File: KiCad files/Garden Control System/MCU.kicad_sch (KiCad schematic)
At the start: 24 parts, among them SW1 SW_SPDT, U1 STM32F207ZGTx, Y1 16MHz

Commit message: Close to finishing ethernet side
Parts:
- removed Y1: 16MHz, symbol Device:Crystal_GND24
- added R1: 0, symbol Device:R
- added Y1: ECS-160-8-37-CWY-TR3, ECS-160-8-37-CWY-TR3:XTAL_ECS-160-8-37-CWY-TR3, symbol ECS-160-8-37-CWY-TR3:ECS-160-8-37-CWY-TR3
- renumbered C1 to C10, C1 to C11, C1 to C12, C1 to C13, C2 to C14, C1 to C15, C1 to C16, C1 to C17, C1 to C18, C1 to C19, C1 to C2, C1 to C3, C1 to C4, C1 to C5, C1 to C6, C1 to C7, C1 to C8, C1 to C9, R1 to R6, SW1 to SW2
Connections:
- net GND: now also Y1.2 (GND), Y1.4 (GND__1)
- net HSE IN: now also Y1.1 (IN/OUT)
- net HSE OUT: now also R1.1; no longer C11.1
- net MII_TXD3: now reaches U1.1 (PE2)
- net MII_MDC: now reaches U1.27 (PC1)
- net MII_TXD2: now reaches U1.28 (PC2)
- net MII_TX_CLK: now reaches U1.29 (PC3)
- net MII_CRS: now reaches U1.34 (PA0)
- net MII_RX_CLK: now reaches U1.35 (PA1)
- net MII_COL: now reaches U1.37 (PA3)
- net MII_RX_DV: now reaches U1.43 (PA7)
- net MII_RX_RD0: now reaches U1.44 (PC4)
- net MII_RX_RD1: now reaches U1.45 (PC5)
- net MII_RX_RD2: now reaches U1.46 (PB0)
- net MII_RX_RD3: now reaches U1.47 (PB1)
- net MII_TXD0: now reaches U1.73 (PB12)
- net MII_TXD1: now reaches U1.74 (PB13)
- new net: C11.1, R1.2, Y1.3 (OUT/IN)
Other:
- moved on the sheet: C11, C12

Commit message: working on power arch
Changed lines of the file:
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@@
+		)
+	)
+	(global_label "MCU_I_SENSE0"
+		(shape input)
+		(at 207.01 124.46 0)
+		(fields_autoplaced yes)
+		(effects
+			(font
+				(size 1.27 1.27)
+			)
+			(justify left)
+		)
+		(property "Intersheetrefs" "${INTERSHEET_REFS}"
+			(at 223.8441 124.46 0)
+			(effects
+				(font
+					(size 1.27 1.27)
+				)
+				(justify left)
+				(hide yes)
+			)
 		)
 	)
@@
 		)
 	)
+	(global_label "MCU_I_SENSE2"
+		(shape input)
+		(at 207.01 129.54 0)
+		(fields_autoplaced yes)
+		(effects
+			(font
+				(size 1.27 1.27)
+			)
+			(justify left)
+		)
+		(property "Intersheetrefs" "${INTERSHEET_REFS}"
+			(at 223.8441 129.54 0)
+			(effects
+				(font
+					(size 1.27 1.27)
+				)
+				(justify left)
+				(hide yes)
+			)
+		)
+	)
+	(global_label "M1_PWM"
+		(shape input)
+		(at 207.01 111.76 0)
+		(fields_autoplaced yes)
+		(effects
+			(font
+				(size 1.27 1.27)
+			)
+			(justify left)
+		)
+		(property "Intersheetrefs" "${INTERSHEET_REFS}"
+			(at 217.7965 111.76 0)
+			(effects
+				(font
+					(size 1.27 1.27)
+				)
+				(justify left)
+				(hide yes)
+			)
+		)
+	)
 	(global_label "MII_RX_RD2"
 		(shape input)
@@
 		)
 	)
+	(global_label "M0_PWM"
+		(shape input)
+		(at 207.01 109.22 0)
+		(fields_autoplaced yes)
+		(effects
+			(font
+				(size 1.27 1.27)
+			)
+			(justify left)
+		)
+		(property "Intersheetrefs" "${INTERSHEET_REFS}"
+			(at 217.7965 109.22 0)
+			(effects
+				(font
+					(size 1.27 1.27)
+				)
+				(justify left)
+				(hide yes)
+			)
+		)
+	)
 	(global_label "HSE OUT"
 		(shape input)
@@
 			(effects
 				(font
+					(size 1.27 1.27)
+				)
+				(justify left)
+				(hide yes)
+			)
+		)
+	)
+	(global_label "MCU_I_SENSE3"
+		(shape input)
+		(at 207.01 132.08 0)
+		(fields_autoplaced yes)
+		(effects
+			(font
+				(size 1.27 1.27)
+			)
+			(justify left)
+		)
+		(property "Intersheetrefs" "${INTERSHEET_REFS}"
+			(at 223.8441 132.08 0)
+			(effects
+				(font
+					(size 1.27 1.27)
+				)
+				(justify left)
+				(hide yes)
+			)
+		)
+	)
+	(global_label "M2_PWM"
+		(shape input)
+		(at 207.01 114.3 0)
+		(fields_autoplaced yes)
+		(effects
+			(font
+				(size 1.27 1.27)
+			)
+			(justify left)
+		)
+		(property "Intersheetrefs" "${INTERSHEET_REFS}"
+			(at 217.7965 114.3 0)
+			(effects
+				(font
+					(size 1.27 1.27)
+				)
+				(justify left)
+				(hide yes)
+			)
+		)
+	)
+	(global_label "MCU_I_SENSE1"
+		(shape input)
+		(at 207.01 127 0)
+		(fields_autoplaced yes)
+		(effects
+			(font
+				(size 1.27 1.27)
+			)
+			(justify left)
+		)
+		(property "Intersheetrefs" "${INTERSHEET_REFS}"
+			(at 223.8441 127 0)
+			(effects
+				(font

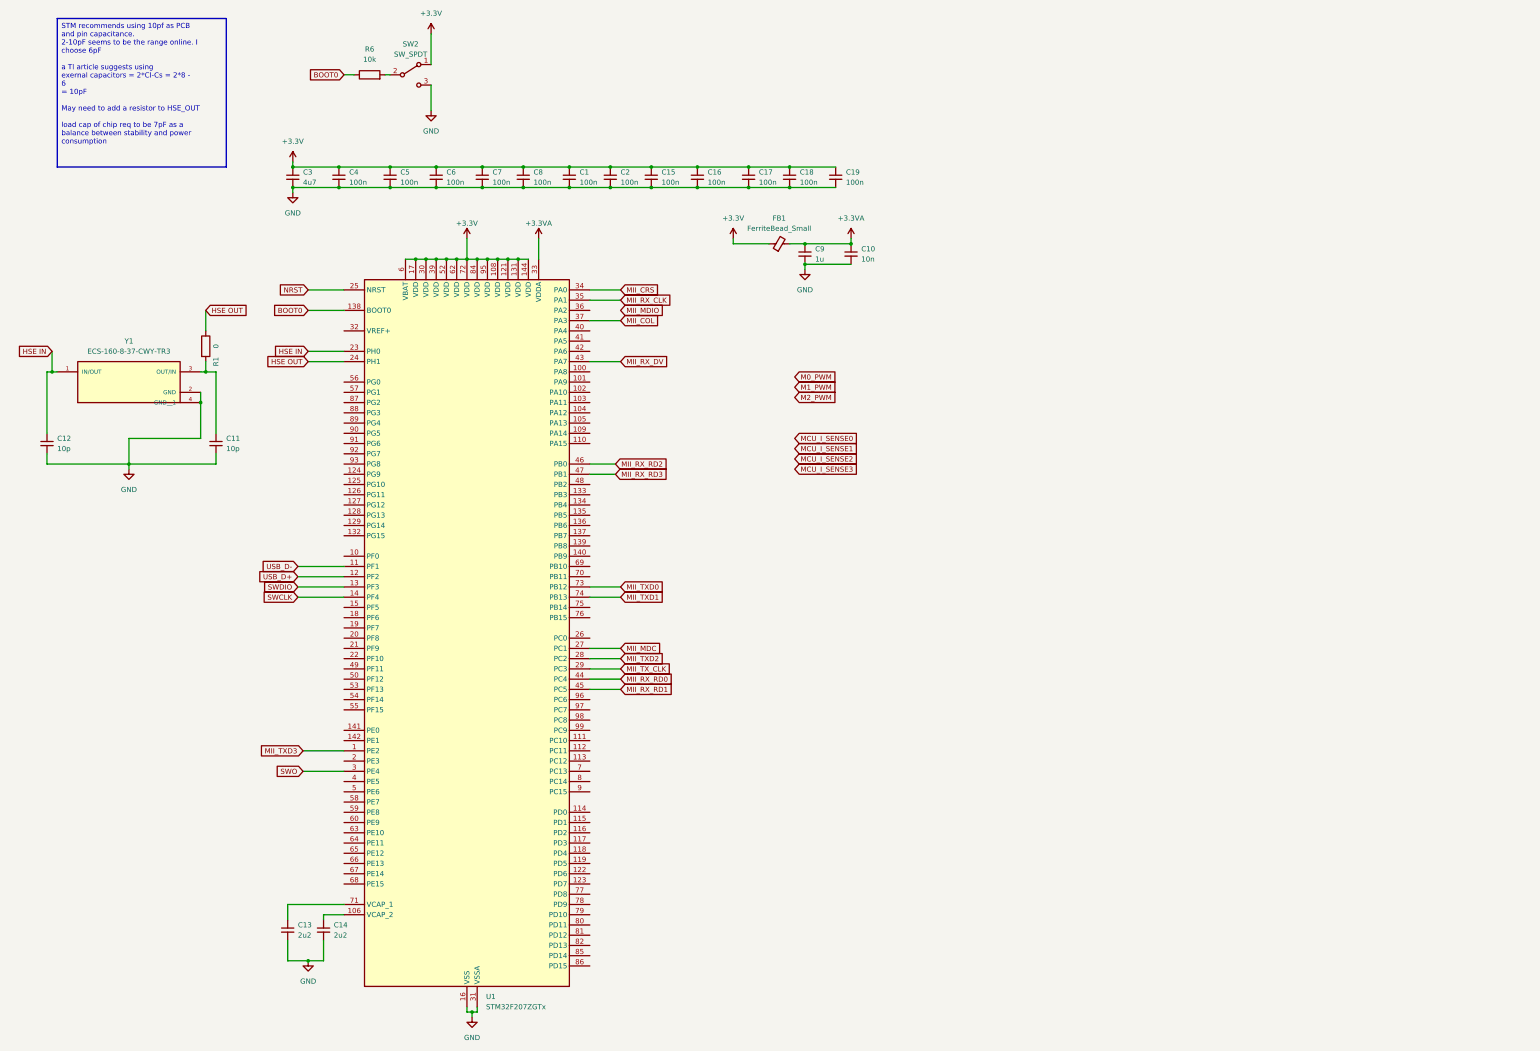
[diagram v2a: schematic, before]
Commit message: expanded power supply section. completed LSD design. sized shunt resistors
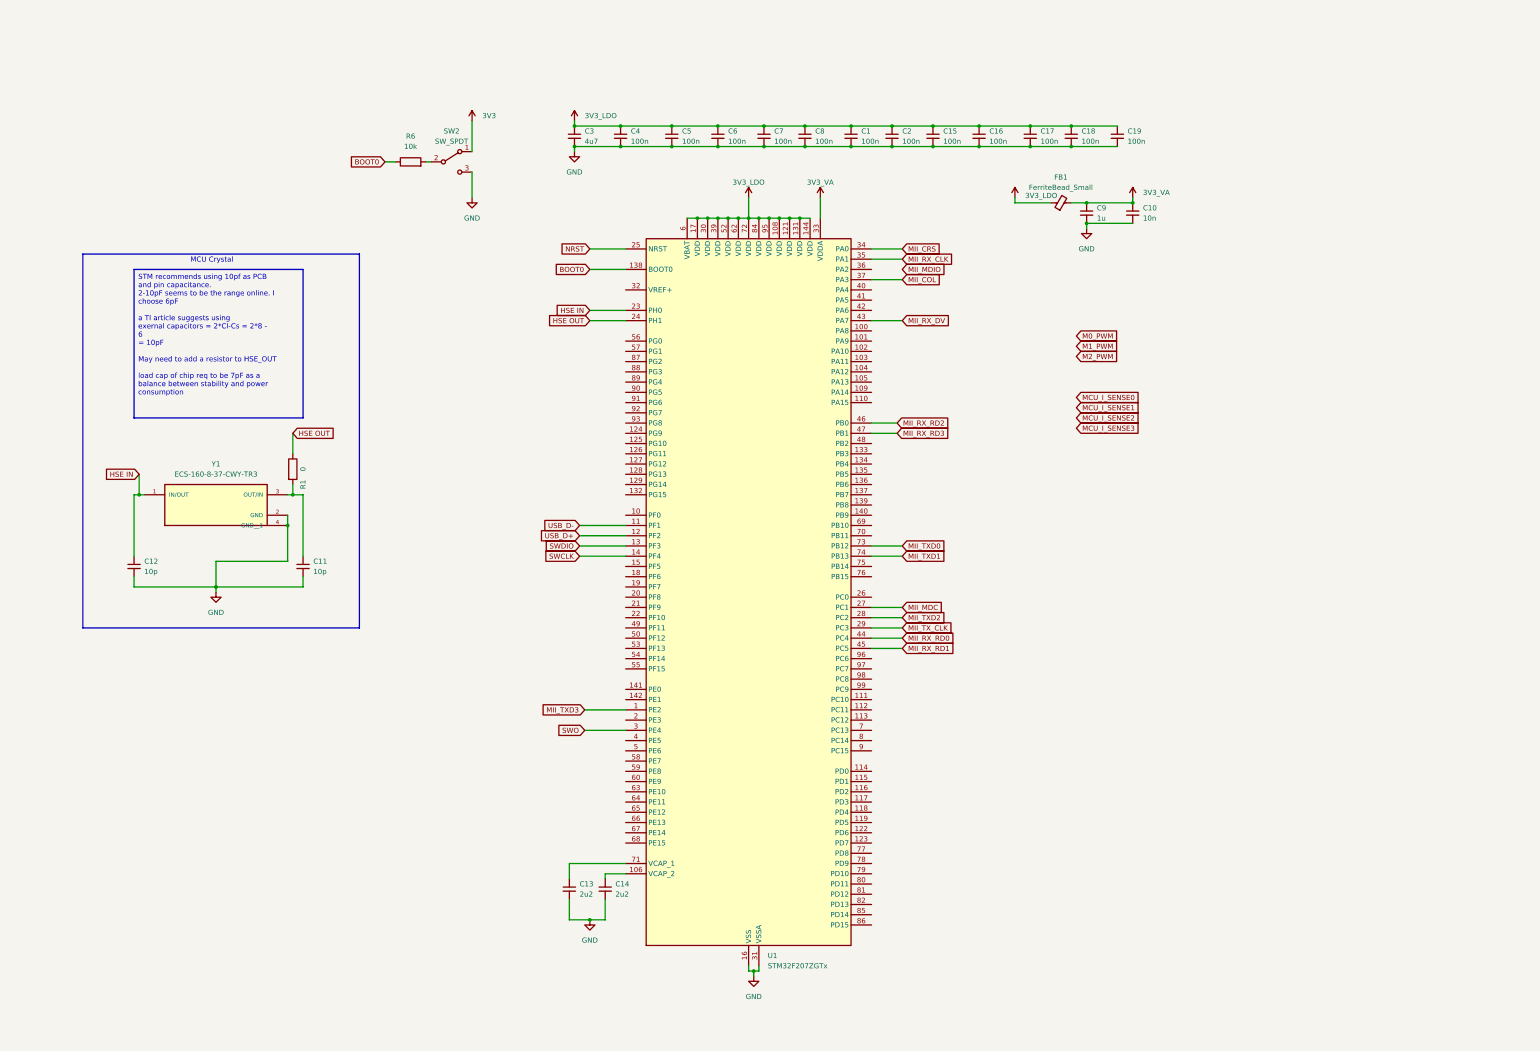
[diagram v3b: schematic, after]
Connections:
- net +3.3V renamed 3V3_LDO
- net 3V3_LDO: no longer SW2.1 (A)
- net +3.3VA renamed 3V3_VA
- new net 3V3: SW2.1 (A)
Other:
- note added: "MCU Crystal"
- moved on the sheet: C1, C10, C11, C12, C13, C14, C15, C16, C17, C18, C19, C2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

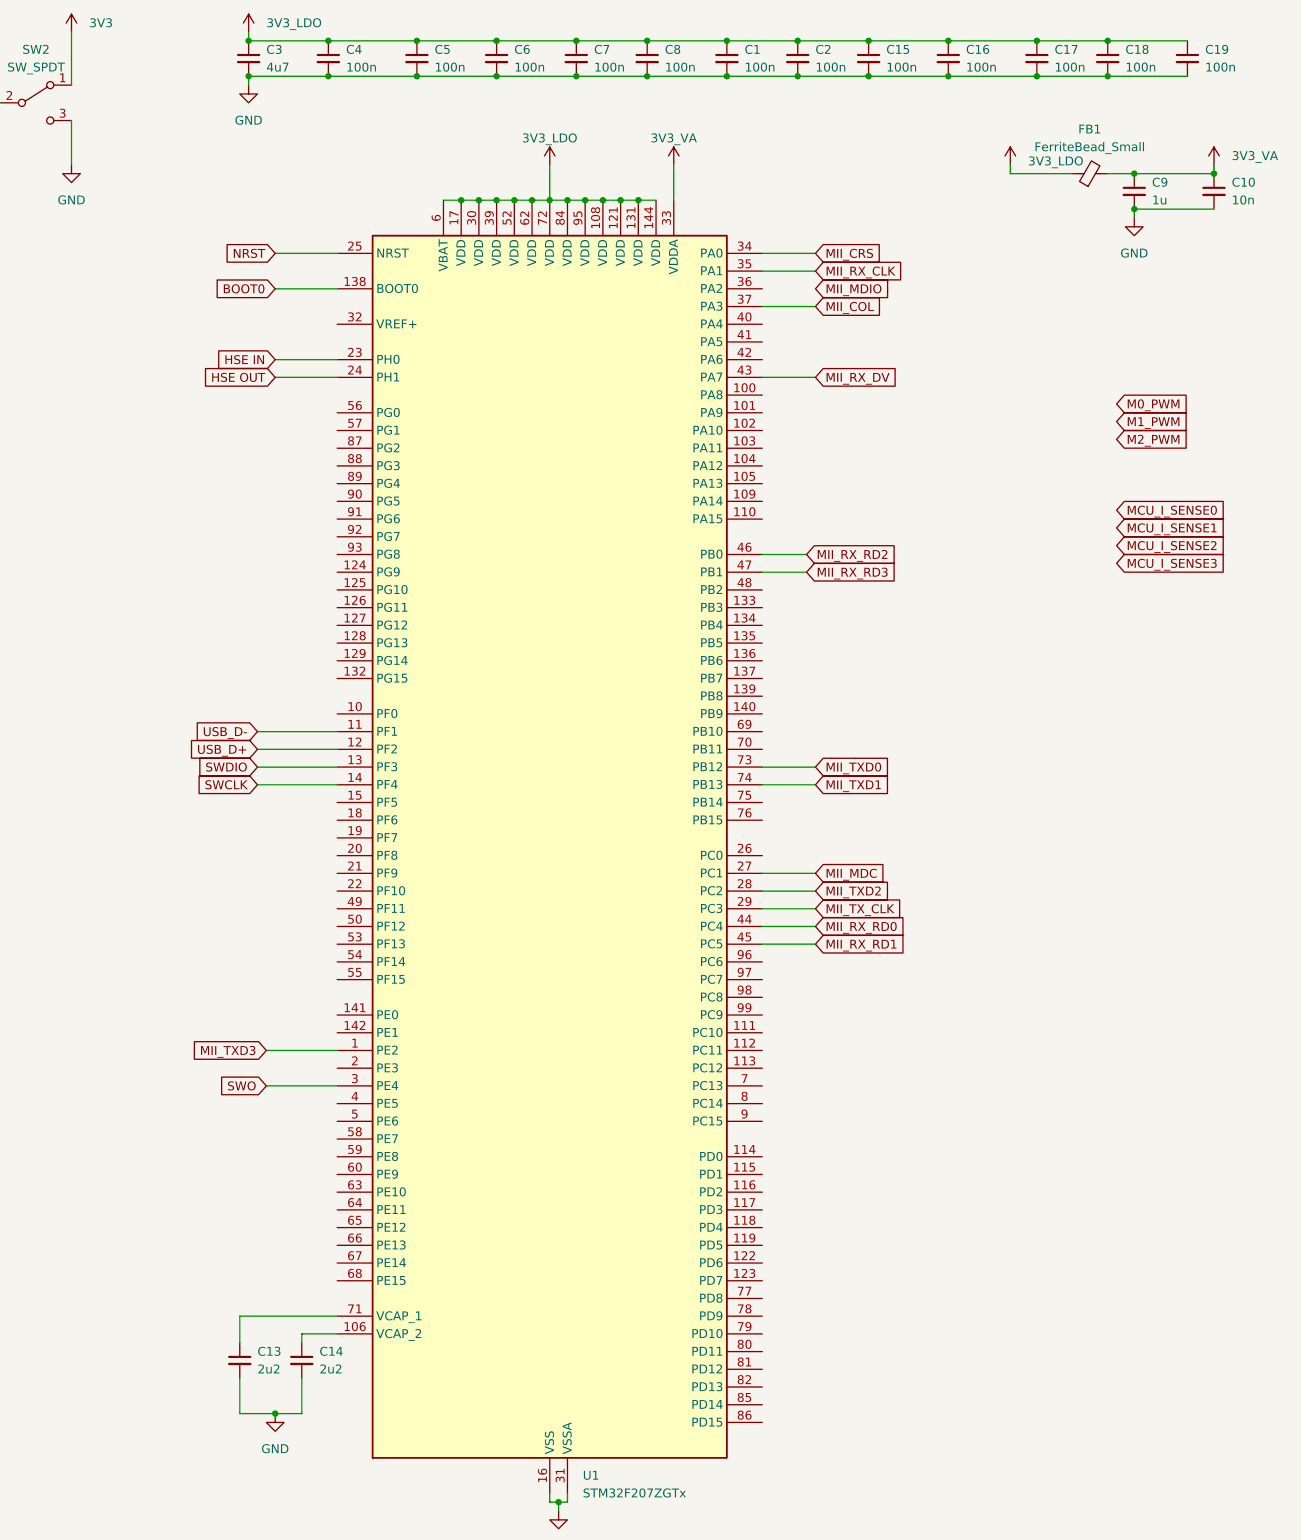
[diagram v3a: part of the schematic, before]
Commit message: adding recent schematic progress
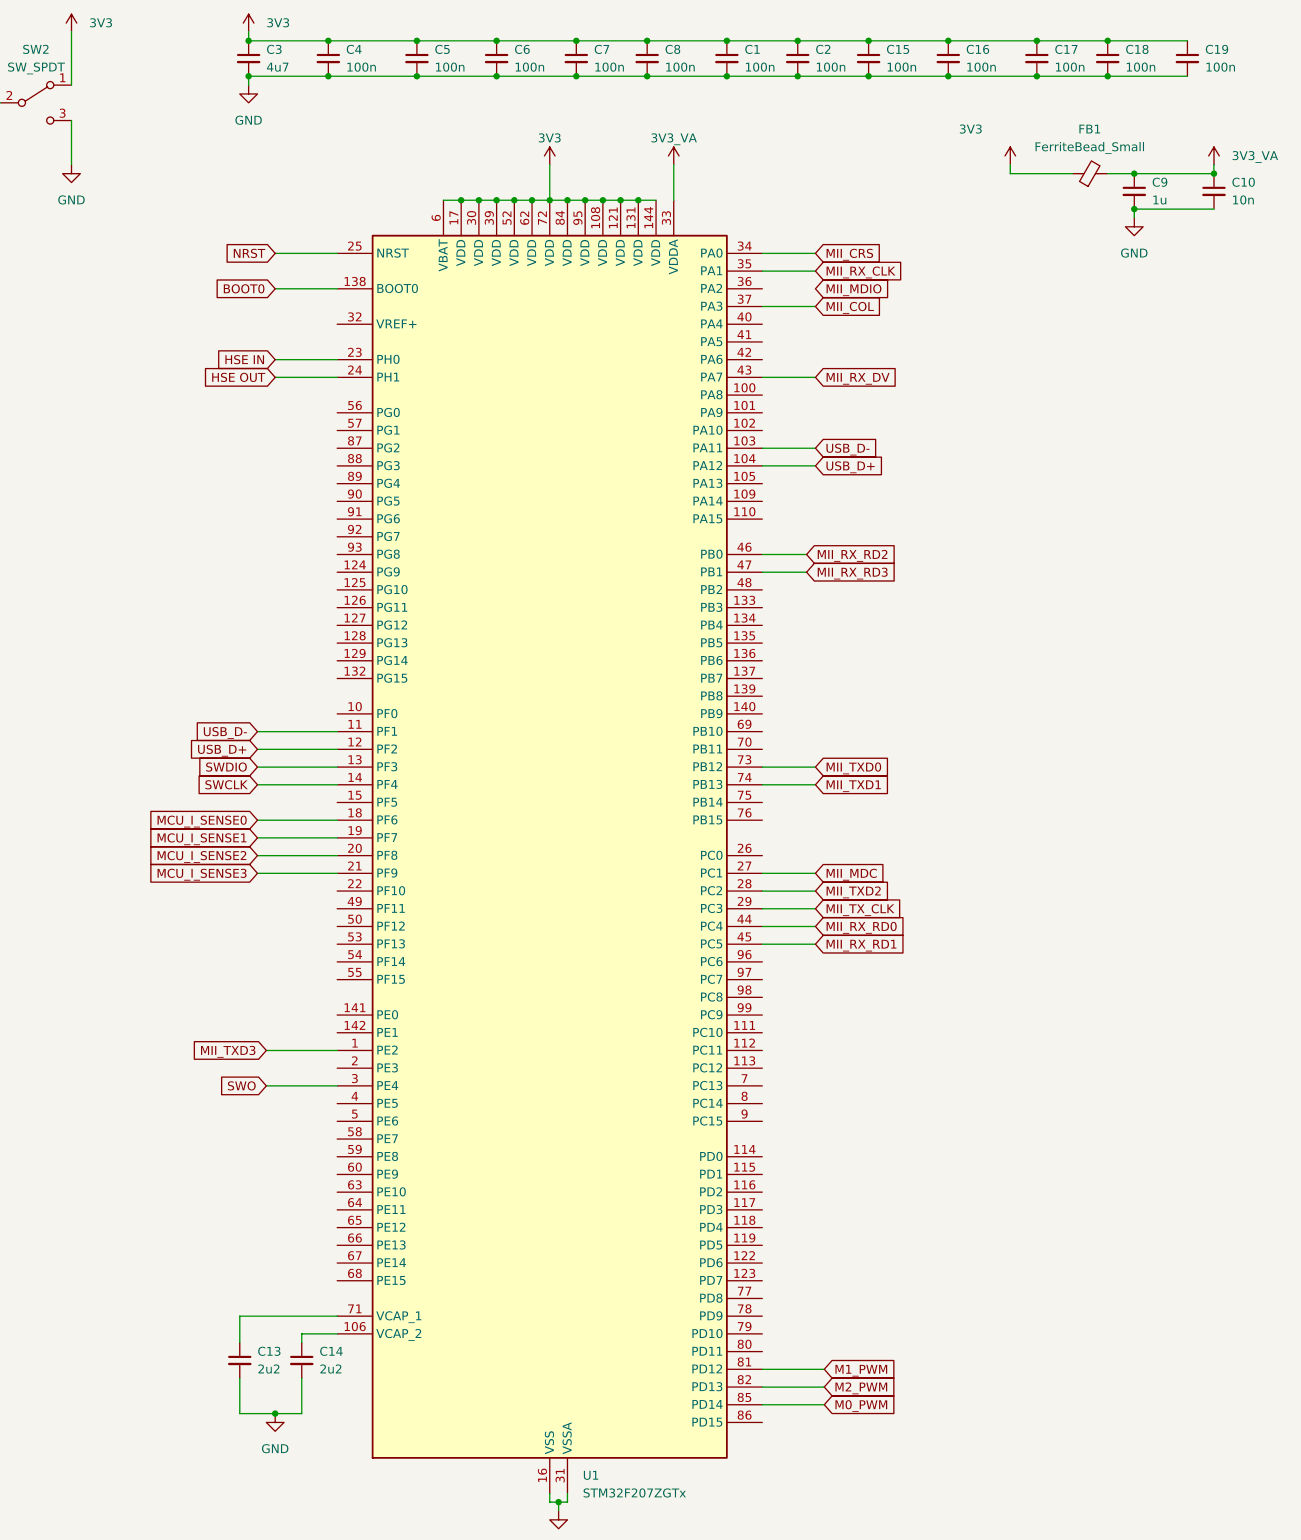
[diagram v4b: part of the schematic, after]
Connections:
- net 3V3_LDO is gone; now on net 3V3: C1.1, C15.1, C16.1, C17.1, C18.1, C19.1, C2.1, C3.1, C4.1, C5.1, C6.1, C7.1, C8.1, FB1.1, U1.108 (VDD), U1.121 (VDD), U1.131 (VDD), U1.144 (VDD), U1.17 (VDD), U1.30 (VDD), U1.39 (VDD), U1.52 (VDD), U1.6 (VBAT), U1.62 (VDD), U1.72 (VDD), U1.84 (VDD), U1.95 (VDD)
- net M0_PWM: now also U1.85 (PD14)
- net M1_PWM: now also U1.81 (PD12)
- net M2_PWM: now also U1.82 (PD13)
- net MCU_I_SENSE0: now also U1.18 (PF6)
- net MCU_I_SENSE1: now also U1.19 (PF7)
- net MCU_I_SENSE2: now also U1.20 (PF8)
- net MCU_I_SENSE3: now also U1.21 (PF9)
- net USB_D+: now also U1.104 (PA12)
- net USB_D-: now also U1.103 (PA11)

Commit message: working on temp sensor circuit
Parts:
- added D4: 3V3 LED, symbol Device:LED_Small
- added R39: 1k47, symbol Device:R_Small
- C13, C14: value 2u2 -> 100n
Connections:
- net GND: now also R39.2
- net HSE IN renamed HSE_IN
- net HSE OUT renamed HSE_OUT
- new net: D4.1 (K), R39.1
- new net DEBUG_LED: D4.2 (A)
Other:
- note added: ""When bypassing the voltage regulator, the two 2.2 μF V CAP capacitors are not required and must be replaced by two 100 nF decoupling capacitors.""
- note added: "LED SML-P11UTT86R Vfw = 1.8, I = 1mA"

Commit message: we cookin' again. Added LSD and start temp sense section.
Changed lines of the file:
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@@
 	)
 	(rectangle
-		(start 30.48 78.74)
+		(start 30.48 73.66)
 		(end 99.06 171.45)
 		(stroke
@@
 	(text "MCU Crystal\n"
 		(exclude_from_sim no)
-		(at 57.15 81.026 0)
-		(effects
-			(font
-				(size 1.27 1.27)
+		(at 45.72 80.772 0)
+		(effects
+			(font
+				(size 3.81 3.81)
+				(thickness 0.762)
+				(bold yes)
+				(color 0 0 0 1)
 			)
 			(justify left bottom)
@@
 				(hide yes)
 			)
-		)
-	)
-	(global_label "GDRIVER_EN"
-		(shape input)
-		(at 273.05 138.43 0)
-		(fields_autoplaced yes)
-		(effects
-			(font
-				(size 1.27 1.27)
-			)
-			(justify left)
-		)
-		(property "Intersheetrefs" "${INTERSHEET_REFS}"
-			(at 287.4047 138.43 0)
-			(effects
-				(font
-					(size 1.27 1.27)
-				)
-				(justify left)
-				(hide yes)
-			)

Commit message: we cookin'
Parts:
- C9: value 1u -> 4u7
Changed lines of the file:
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@@
 		(fields_autoplaced yes)
 		(property "Reference" "C9"
-			(at 281.94 67.3163 0)
+			(at 281.94 67.3162 0)
 			(effects
 				(font
@@
 			)
 		)
-		(property "Value" "1u"
-			(at 281.94 69.8563 0)
+		(property "Value" "4u7"
+			(at 281.94 69.8562 0)
 			(effects
 				(font
